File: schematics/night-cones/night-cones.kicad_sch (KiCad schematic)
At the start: 5 parts, among them Q1 Q_NPN_BCE, Q2 Q_NPN_BCE, Q3 Q_NPN_BCE

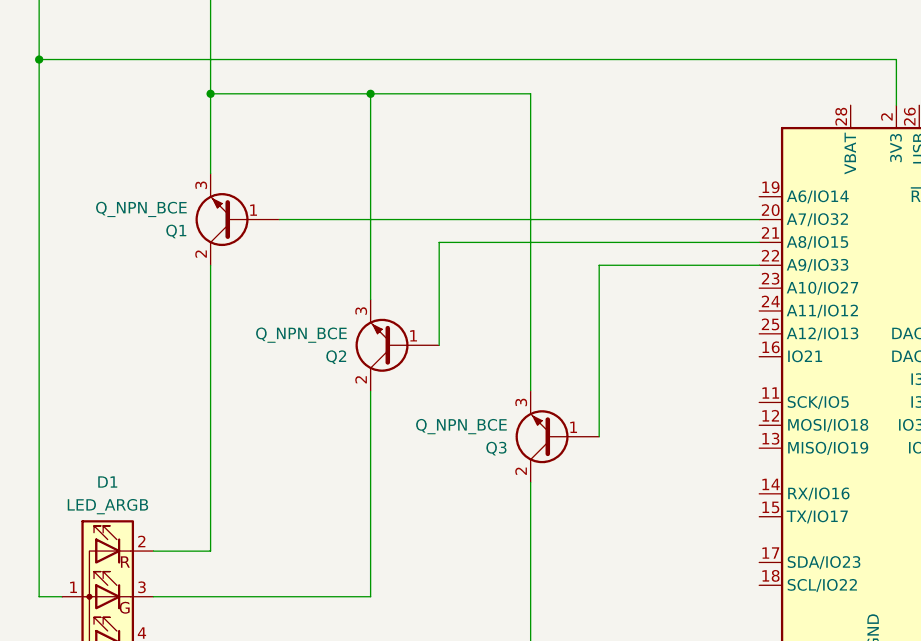
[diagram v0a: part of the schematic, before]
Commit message: Added resistors to gate of mosfet to limit current.
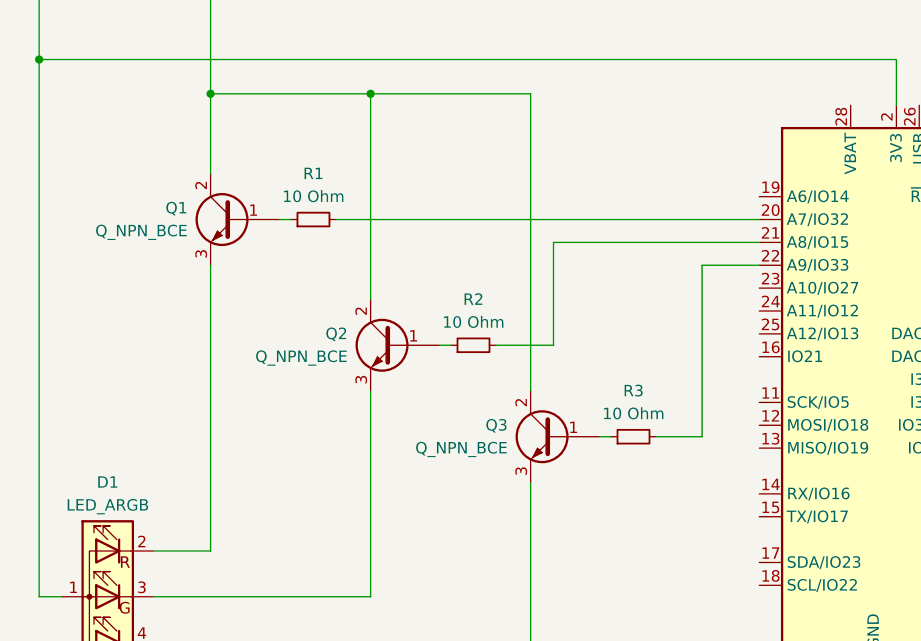
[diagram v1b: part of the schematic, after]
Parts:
- added R1, R2, R3: 10 Ohm, symbol Device:R_Small
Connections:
- net GND: now also Q1.2 (C), Q2.2 (C), Q3.2 (C); no longer Q1.3 (E), Q2.3 (E), Q3.3 (E)
- net at A1.20 (A7/IO32): now also R1.2; no longer Q1.1 (B)
- net at A1.21 (A8/IO15): now also R2.2; no longer Q2.1 (B)
- net at A1.22 (A9/IO33): now also R3.2; no longer Q3.1 (B)
- net at D1.2 (RK): now also Q1.3 (E); no longer Q1.2 (C)
- net at D1.3 (GK): now also Q2.3 (E); no longer Q2.2 (C)
- net at D1.4 (BK): now also Q3.3 (E); no longer Q3.2 (C)
- new net: Q1.1 (B), R1.1
- new net: Q3.1 (B), R3.1
- new net: Q2.1 (B), R2.1
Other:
- moved on the sheet: Q1, Q2, Q3
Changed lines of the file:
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@@
   (junction (at 62.23 45.72) (diameter 0) (color 0 0 0 0)
   )
+  (wire (pts (xy 119.38 66.04) (xy 119.38 77.47))
+    (stroke (width 0) (type default))
+  )
   (wire (pts (xy 116.84 110.49) (xy 116.84 92.71))
     (stroke (width 0) (type default))
@@
     (stroke (width 0) (type default))
   )
+  (wire (pts (xy 135.89 87.63) (xy 135.89 68.58))
+    (stroke (width 0) (type default))
+  )
   (wire (pts (xy 154.94 120.65) (xy 154.94 114.3))
     (stroke (width 0) (type default))
   )
+  (wire (pts (xy 88.9 63.5) (xy 90.17 63.5))
+    (stroke (width 0) (type default))
+  )
   (wire (pts (xy 81.28 49.53) (xy 81.28 58.42))
     (stroke (width 0) (type default))
@@
     (stroke (width 0) (type default))
   )
-  (wire (pts (xy 106.68 66.04) (xy 106.68 77.47))
+  (wire (pts (xy 119.38 66.04) (xy 142.24 66.04))
     (stroke (width 0) (type default))
   )
@@
     (stroke (width 0) (type default))
   )
-  (wire (pts (xy 88.9 63.5) (xy 142.24 63.5))
+  (wire (pts (xy 124.46 87.63) (xy 125.73 87.63))
     (stroke (width 0) (type default))
   )
@@
     (stroke (width 0) (type default))
   )
+  (wire (pts (xy 107.95 77.47) (xy 106.68 77.47))
+    (stroke (width 0) (type default))
+  )
   (wire (pts (xy 81.28 49.53) (xy 99.06 49.53))
     (stroke (width 0) (type default))
   )
+  (wire (pts (xy 135.89 68.58) (xy 142.24 68.58))
+    (stroke (width 0) (type default))
+  )
   (wire (pts (xy 81.28 68.58) (xy 81.28 100.33))
     (stroke (width 0) (type default))
   )
-  (wire (pts (xy 142.24 66.04) (xy 106.68 66.04))
-    (stroke (width 0) (type default))
-  )
   (wire (pts (xy 157.48 45.72) (xy 157.48 50.8))
     (stroke (width 0) (type default))
@@
     (stroke (width 0) (type default))
   )
-  (wire (pts (xy 142.24 68.58) (xy 124.46 68.58))
-    (stroke (width 0) (type default))
-  )
-  (wire (pts (xy 124.46 68.58) (xy 124.46 87.63))
+  (wire (pts (xy 130.81 87.63) (xy 135.89 87.63))
     (stroke (width 0) (type default))
   )
@@
     (stroke (width 0) (type default))
   )
+  (wire (pts (xy 95.25 63.5) (xy 142.24 63.5))
+    (stroke (width 0) (type default))
+  )
   (wire (pts (xy 116.84 49.53) (xy 116.84 82.55))
+    (stroke (width 0) (type default))
+  )
+  (wire (pts (xy 119.38 77.47) (xy 113.03 77.47))
     (stroke (width 0) (type default))
   )
@@
     )
   )
-  (symbol (lib_id "Device:Q_NPN_BCE") (at 83.82 63.5 180) (unit 1)
+  (symbol (lib_id "Device:Q_NPN_BCE") (at 83.82 63.5 0) (mirror y) (unit 1)
     (in_bom yes) (on_board yes) (dnp no)
-    (property "Reference" "Q1" (at 78.74 64.77 0)
-      (effects (font (size 1.27 1.27)) (justify left))
-    )
-    (property "Value" "Q_NPN_BCE" (at 78.74 62.23 0)
-      (effects (font (size 1.27 1.27)) (justify left))
-    )
-    (property "Footprint" "" (at 78.74 66.04 0)
+    (property "Reference" "Q1" (at 78.74 62.23 0)
+      (effects (font (size 1.27 1.27)) (justify left))
+    )
+    (property "Value" "Q_NPN_BCE" (at 78.74 64.77 0)
+      (effects (font (size 1.27 1.27)) (justify left))
+    )
+    (property "Footprint" "" (at 78.74 60.96 0)
       (effects (font (size 1.27 1.27)) hide)
     )
@@
         (path "/03b17979-840b-4ffc-a1b0-c546ee8d29f5"
           (reference "Q1") (unit 1)
+        )
+      )
+    )
+  )
+  (symbol (lib_id "Device:R_Small") (at 128.27 87.63 90) (unit 1)
+    (in_bom yes) (on_board yes) (dnp no) (fields_autoplaced)
+    (property "Reference" "R3" (at 128.27 82.55 90)
+      (effects (font (size 1.27 1.27)))
+    )
+    (property "Value" "10 Ohm" (at 128.27 85.09 90)
+      (effects (font (size 1.27 1.27)))
+    )
+    (property "Footprint" "" (at 128.27 87.63 0)
+      (effects (font (size 1.27 1.27)) hide)
+    )
+    (property "Datasheet" "~" (at 128.27 87.63 0)
+      (effects (font (size 1.27 1.27)) hide)
+    )
+    (pin "1")
+    (pin "2")
+    (instances
+      (project "night-cones"
+        (path "/03b17979-840b-4ffc-a1b0-c546ee8d29f5"
+          (reference "R3") (unit 1)
+        )
+      )
+    )
+  )
+  (symbol (lib_id "Device:R_Small") (at 92.71 63.5 90) (unit 1)
+    (in_bom yes) (on_board yes) (dnp no) (fields_autoplaced)
+    (property "Reference" "R1" (at 92.71 58.42 90)
+      (effects (font (size 1.27 1.27)))
+    )
+    (property "Value" "10 Ohm" (at 92.71 60.96 90)
+      (effects (font (size 1.27 1.27)))
+    )
+    (property "Footprint" "" (at 92.71 63.5 0)
+      (effects (font (size 1.27 1.27)) hide)
+    )
+    (property "Datasheet" "~" (at 92.71 63.5 0)
+      (effects (font (size 1.27 1.27)) hide)
+    )
+    (pin "1")
+    (pin "2")
+    (instances
+      (project "night-cones"
+        (path "/03b17979-840b-4ffc-a1b0-c546ee8d29f5"
+          (reference "R1") (unit 1)
         )
       )
@@
     )
   )
-  (symbol (lib_id "Device:Q_NPN_BCE") (at 101.6 77.47 180) (unit 1)
+  (symbol (lib_id "Device:Q_NPN_BCE") (at 101.6 77.47 0) (mirror y) (unit 1)
     (in_bom yes) (on_board yes) (dnp no)
-    (property "Reference" "Q2" (at 96.52 78.74 0)
-      (effects (font (size 1.27 1.27)) (justify left))
-    )
-    (property "Value" "Q_NPN_BCE" (at 96.52 76.2 0)
-      (effects (font (size 1.27 1.27)) (justify left))
-    )
-    (property "Footprint" "" (at 96.52 80.01 0)
+    (property "Reference" "Q2" (at 96.52 76.2 0)
+      (effects (font (size 1.27 1.27)) (justify left))
+    )
+    (property "Value" "Q_NPN_BCE" (at 96.52 78.74 0)
+      (effects (font (size 1.27 1.27)) (justify left))
+    )
+    (property "Footprint" "" (at 96.52 74.93 0)
       (effects (font (size 1.27 1.27)) hide)
     )
@@
     )
   )
-  (symbol (lib_id "Device:Q_NPN_BCE") (at 119.38 87.63 180) (unit 1)
+  (symbol (lib_id "Device:Q_NPN_BCE") (at 119.38 87.63 0) (mirror y) (unit 1)
     (in_bom yes) (on_board yes) (dnp no)
-    (property "Reference" "Q3" (at 114.3 88.9 0)
-      (effects (font (size 1.27 1.27)) (justify left))
-    )
-    (property "Value" "Q_NPN_BCE" (at 114.3 86.36 0)
-      (effects (font (size 1.27 1.27)) (justify left))
-    )
-    (property "Footprint" "" (at 114.3 90.17 0)
+    (property "Reference" "Q3" (at 114.3 86.36 0)
+      (effects (font (size 1.27 1.27)) (justify left))
+    )
+    (property "Value" "Q_NPN_BCE" (at 114.3 88.9 0)
+      (effects (font (size 1.27 1.27)) (justify left))
+    )
+    (property "Footprint" "" (at 114.3 85.09 0)
       (effects (font (size 1.27 1.27)) hide)
     )
@@
         )
       )
+    )
+  )
+  (symbol (lib_id "Device:R_Small") (at 110.49 77.47 90) (unit 1)
+    (in_bom yes) (on_board yes) (dnp no) (fields_autoplaced)
+    (property "Reference" "R2" (at 110.49 72.39 90)
+      (effects (font (size 1.27 1.27)))
+    )
+    (property "Value" "10 Ohm" (at 110.49 74.93 90)
+      (effects (font (size 1.27 1.27)))
+    )
+    (property "Footprint" "" (at 110.49 77.47 0)
+      (effects (font (size 1.27 1.27)) hide)
+    )
+    (property "Datasheet" "~" (at 110.49 77.47 0)
+      (effects (font (size 1.27 1.27)) hide)
+    )
+    (pin "1")
+    (pin "2")
+    (instances
+      (project "night-cones"
+        (path "/03b17979-840b-4ffc-a1b0-c546ee8d29f5"
+          (reference "R2") (unit 1)
+        )
+      )

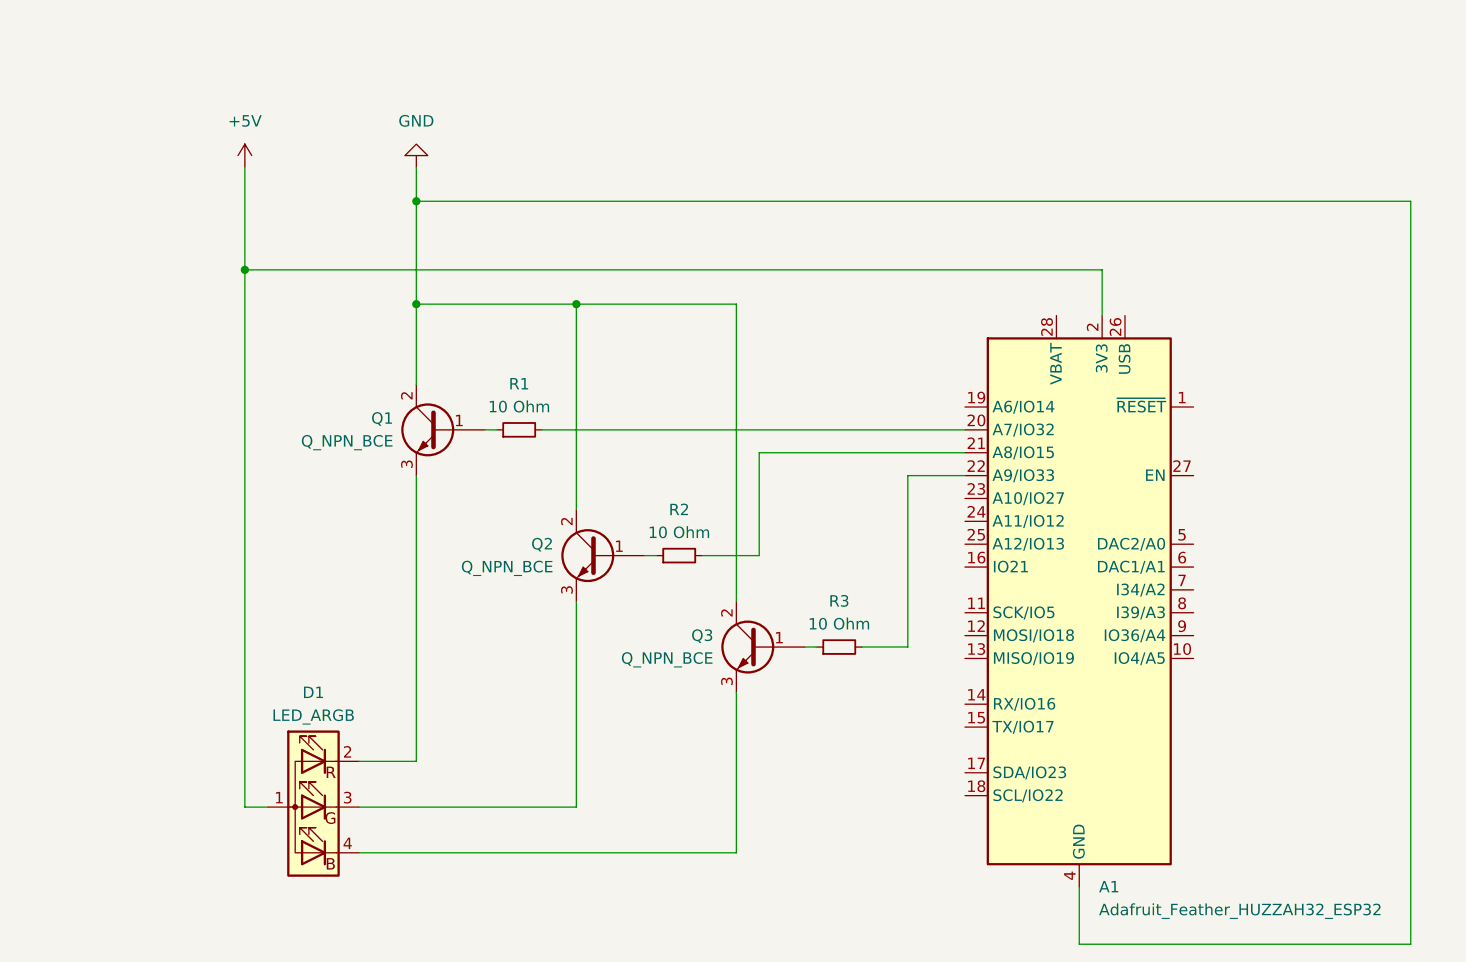
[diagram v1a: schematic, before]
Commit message: Added CAD files. Modified .gitignore
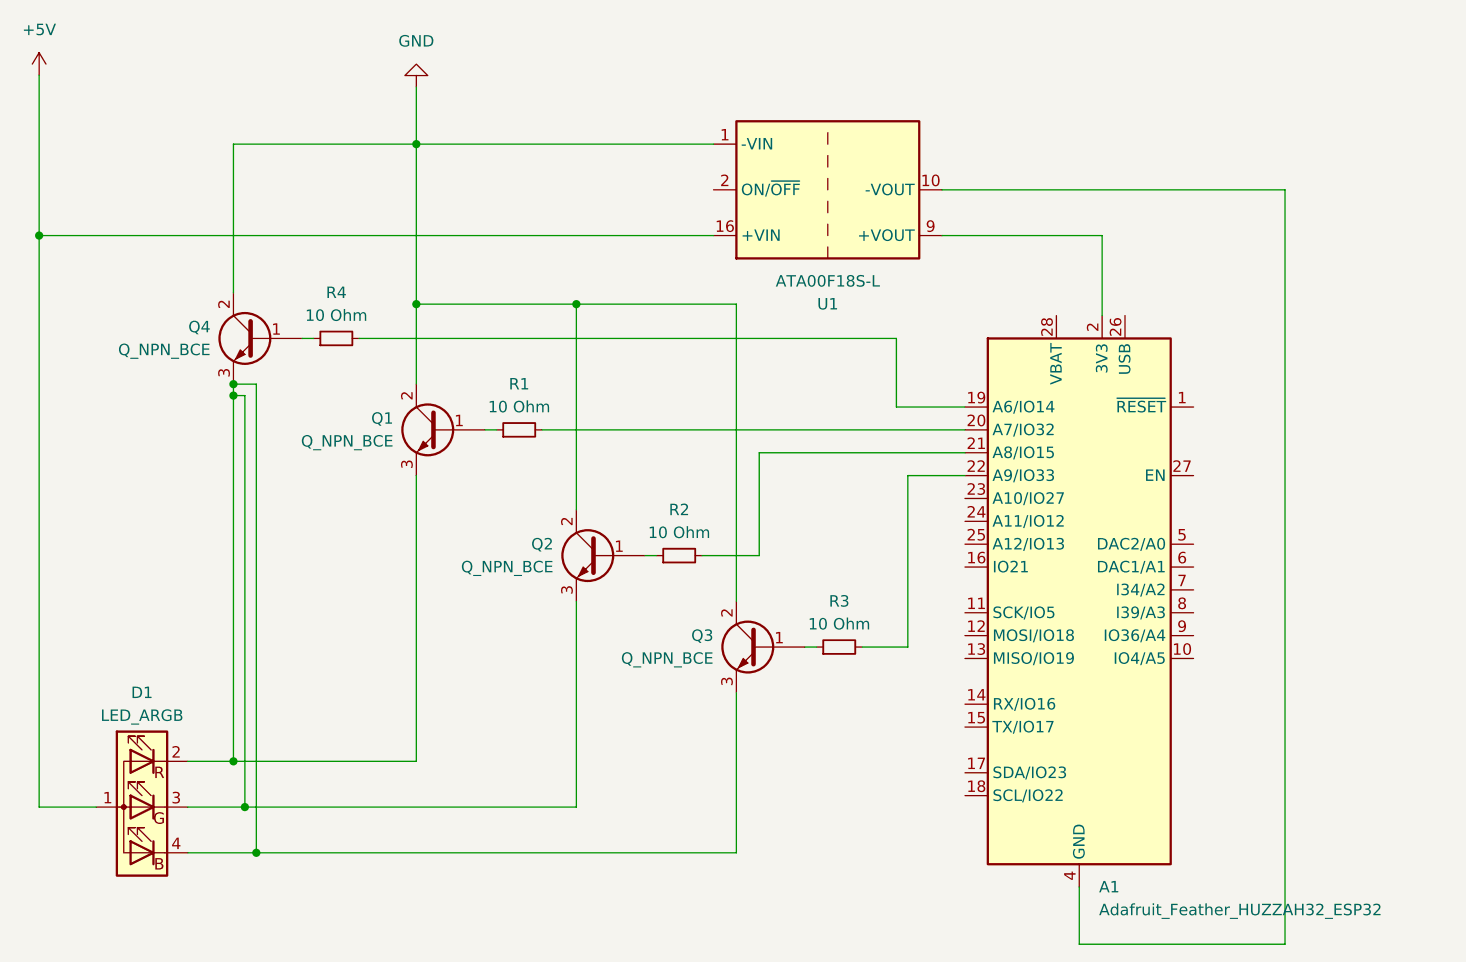
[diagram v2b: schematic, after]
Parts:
- added Q4: Q_NPN_BCE, symbol Device:Q_NPN_BCE
- added R4: 10 Ohm, symbol Device:R_Small
- added U1: ATA00F18S-L, Converter_DCDC:Converter_DCDC_Artesyn_ATA_SMD, symbol Converter_DCDC:ATA00F18S-L
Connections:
- net +5V: now also U1.16 (+VIN); no longer A1.2 (3V3)
- net GND: now also Q4.2 (C), U1.1 (-VIN); no longer A1.4 (GND)
- net at A1.19 (A6/IO14): now also R4.2
- net at D1.2 (RK), Q1.3 (E): now also D1.3 (GK), D1.4 (BK), Q2.3 (E), Q3.3 (E), Q4.3 (E)
- new net: A1.2 (3V3), U1.9 (+VOUT)
- new net: A1.4 (GND), U1.10 (-VOUT)
- new net: Q4.1 (B), R4.1
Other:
- moved on the sheet: D1
